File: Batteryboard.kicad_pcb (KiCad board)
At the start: 4 copper layers, 76.2 x 76.2 mm, 173 parts, among them IC1 FAN4010IL6X_F113, IC2 FAN4010IL6X_F113, IC3 FAN4010IL6X_F113, J1 Conn_01x02_Male, J2 Conn_01x03_Male, J3 Conn_01x05_Male, J4 Conn_01x02_Male, J5 SC_19-20, J6 Conn_01x04_Male, Q1 SI7617DN-T1-GE3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

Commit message: addede pms silkscreen
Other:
- board text added: "PMS Rev0"
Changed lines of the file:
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@@
   (general
     (thickness 1.6)
-    (drawings 6)
+    (drawings 7)
     (tracks 1505)
     (zones 0)
@@
   (page A4)
   (layers
-    (0 F.Cu signal)
-    (1 In1.Cu power)
-    (2 In2.Cu signal)
-    (31 B.Cu power)
+    (0 F.Cu signal hide)
+    (1 In1.Cu power hide)
+    (2 In2.Cu signal hide)
+    (31 B.Cu power hide)
     (32 B.Adhes user)
     (33 F.Adhes user)
@@
     )
   )
+  (gr_text "PMS Rev0" (at 249.1232 50.7492) (layer B.SilkS)
+    (effects (font (size 1.524 1.524) (thickness 0.254)) (justify mirror))
+  )
   (gr_circle (center 235.3818 63.0682) (end 273.1262 57.9882) (layer Edge.Cuts) (width 0.05))

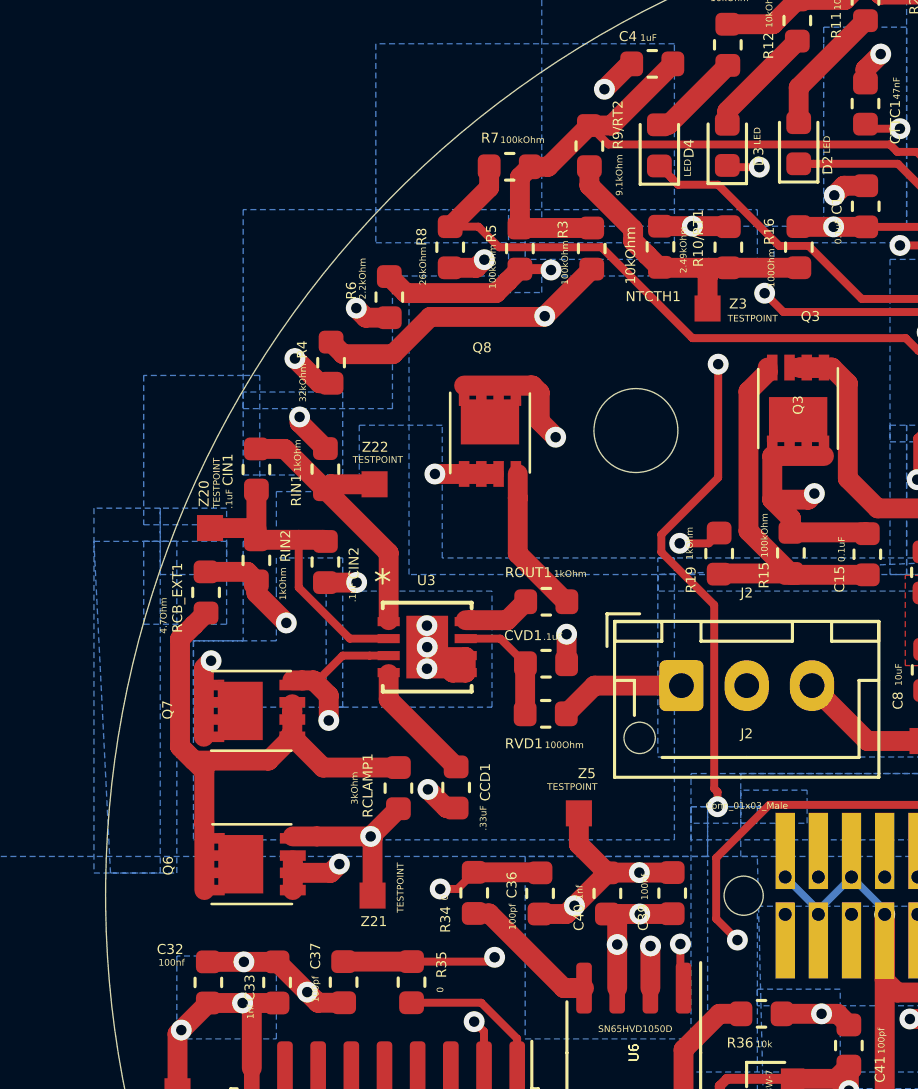
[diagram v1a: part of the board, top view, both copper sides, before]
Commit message: changed up balancing circuit cuz that no work and that bad
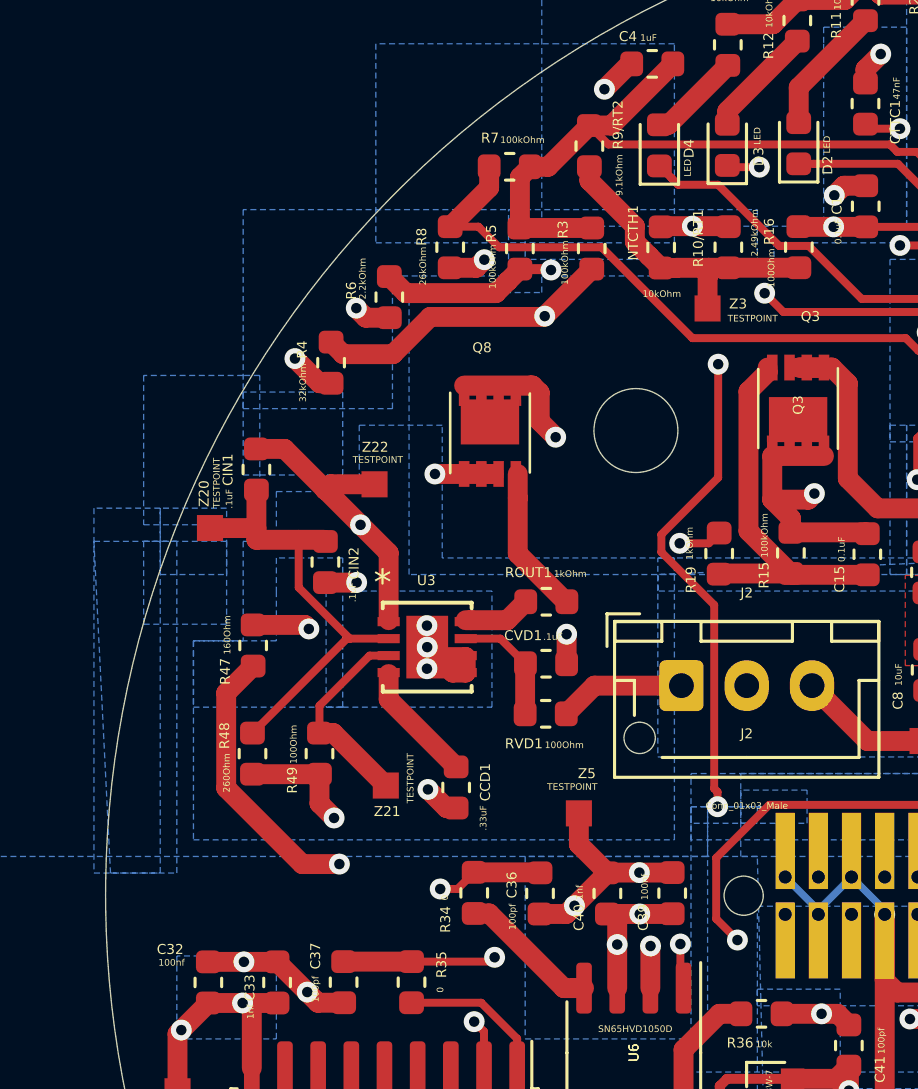
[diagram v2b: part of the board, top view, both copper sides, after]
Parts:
- removed Q6: SIS412DN-T1-GE3, SI7617DN-T1-GE3:SIS862DNT1GE3
- removed Q7: SI7617DN-T1-GE3, SI7617DN-T1-GE3:SIS862DNT1GE3
- removed RCB_EXT1: 4.7Ohm, Resistor_SMD:R_0603_1608Metric
- removed RCLAMP1: 3kOhm, Resistor_SMD:R_0603_1608Metric
- removed RIN1, RIN2: 1kOhm, Resistor_SMD:R_0603_1608Metric
- added R47: 160Ohm, Resistor_SMD:R_0603_1608Metric, F.Cu at (202.9, 53.5)
- added R48: 260Ohm, Resistor_SMD:R_0603_1608Metric, F.Cu at (202.9, 57.7)
- added R49: 100Ohm, Resistor_SMD:R_0603_1608Metric, F.Cu at (205.5, 57.7)
- moved Z21 4.24 mm to (208.0, 55.9)
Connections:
- net Q6G renamed Net-(R49-Pad1)
- net Q6S renamed Net-(F2-Pad2)
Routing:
- net Q6D: track 22.2 -> 0.00 mm
- net Net-(F2-Pad2): track 90.4 -> 76.5 mm, vias 2 -> 1
- net Net-(R49-Pad1): track 18.6 -> 7.86 mm, vias 2 -> 0
- net Net-(CIN1-Pad1): track 11.3 -> 18.3 mm, vias 0 -> 2
- net Net-(CIN1-Pad2): track 12.4 -> 17.7 mm
- net PGND2: track 75.1 -> 72.2 mm, vias 32 -> 31
- net Net-(J2-Pad2): track 25.1 -> 23.9 mm

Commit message: made some finishing touches, should be complete now
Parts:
- removed the C23 at (239.5, 96.9)
- removed the C31 at (220.5, 96.0)
- removed the C45 at (235.2, 99.3)
- removed the C46 at (224.9, 97.4)
- removed the C48 at (220.5, 92.6)
- removed the C49 at (227.0, 94.0)
- R48: value 260Ohm -> 261Ohm
- moved Z15 2.57 mm to (220.5, 88.7)
- renumbered NTCTH1 to NTCTH1/NTCG163JF103FT1S1
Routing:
- net 5V0: track 43.3 -> 39.7 mm
- net VSS: track 137.8 -> 134.4 mm
- net TEMP_OUT: track 15.3 -> 12.8 mm

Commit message: fixed stuff
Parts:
- removed J5: SC_19-20, MASA-LIB:bottom_Stack_Connector_2019_2020
- added J7: SC_19-20, MASA_Library:Stack_Connector_2019_2020, F.Cu at (235.4, 63.1)
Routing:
- net VSS: track 134.4 -> 122.0 mm
- net 5V0: track 39.7 -> 31.2 mm, vias 15 -> 14
- net CAN_L: track 36.7 -> 34.6 mm, vias 3 -> 2
- net CAN_H: track 33.2 -> 31.1 mm, vias 3 -> 2
- net 3V3: vias 3 -> 2
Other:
- net class Default: clearance 0.15 -> 0.1524
- rule trace_clearance: 0.15 -> 0.1524

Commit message: fixed some shit
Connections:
- IC1 pad 2: Net-(IC1-Pad2) -> (no net)
- IC1 pad 4: Net-(IC1-Pad4) -> (no net)
- IC2 pad 2: Net-(IC2-Pad2) -> (no net)
- IC2 pad 4: Net-(IC2-Pad4) -> (no net)
- IC3 pad 2: Net-(IC3-Pad2) -> (no net)
- IC3 pad 4: Net-(IC3-Pad4) -> (no net)
- J7 pad 1: VSS -> PGND2
- J7 pad 10: Net-(J7-Pad10) -> (no net)
- J7 pad 11: Net-(J7-Pad11) -> (no net)
- J7 pad 12: Net-(J7-Pad12) -> (no net)
- J7 pad 13: Net-(J7-Pad13) -> (no net)
- J7 pad 14: Net-(J7-Pad14) -> (no net)
- J7 pad 15: Net-(J7-Pad15) -> (no net)
- J7 pad 16: Net-(J7-Pad16) -> (no net)
- J7 pad 17: Net-(J7-Pad17) -> (no net)
- J7 pad 18: Net-(J7-Pad18) -> (no net)
- J7 pad 19: VSS -> PGND2
- J7 pad 20: VSS -> PGND2
- J7 pad 22: Net-(J7-Pad22) -> (no net)
- J7 pad 24: Net-(J7-Pad24) -> (no net)
- J7 pad 25: UART1_TX -> (no net)
- J7 pad 26: Net-(J7-Pad26) -> (no net)
- J7 pad 27: UART1_RX -> (no net)
- J7 pad 28: Net-(J7-Pad28) -> (no net)
- J7 pad 29: Net-(J7-Pad29) -> (no net)
- J7 pad 30: Net-(J7-Pad30) -> (no net)
- J7 pad 31: Net-(J7-Pad31) -> (no net)
- J7 pad 32: Net-(J7-Pad32) -> (no net)
- J7 pad 33: Net-(J7-Pad33) -> (no net)
- J7 pad 36: VSS -> PGND2
- J7 pad 37: VSS -> PGND2
- J7 pad 4: VSS -> PGND2
- J7 pad 40: VSS -> PGND2
- J7 pad 5: VSS -> PGND2
- J7 pad 8: Net-(J7-Pad8) -> (no net)
- J7 pad 9: Net-(J7-Pad9) -> (no net)
- U2 pad 12: Net-(U2-Pad12) -> (no net)
- U2 pad 13: Net-(U2-Pad13) -> (no net)
- U4 pad 15: Net-(U4-Pad15) -> (no net)
- U4 pad 16: Net-(U4-Pad16) -> (no net)
- U5 pad 3: Net-(U5-Pad3) -> (no net)
- U5 pad 7: Net-(U5-Pad7) -> (no net)
- U5 pad 8: Net-(U5-Pad8) -> (no net)
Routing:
- net VSS: track 122.0 -> 145.3 mm, vias 54 -> 52
- net PGND2: track 72.2 -> 85.0 mm
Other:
- net class Default: clearance 0.1524 -> 0.14986
- rule trace_clearance: 0.1524 -> 0.14986

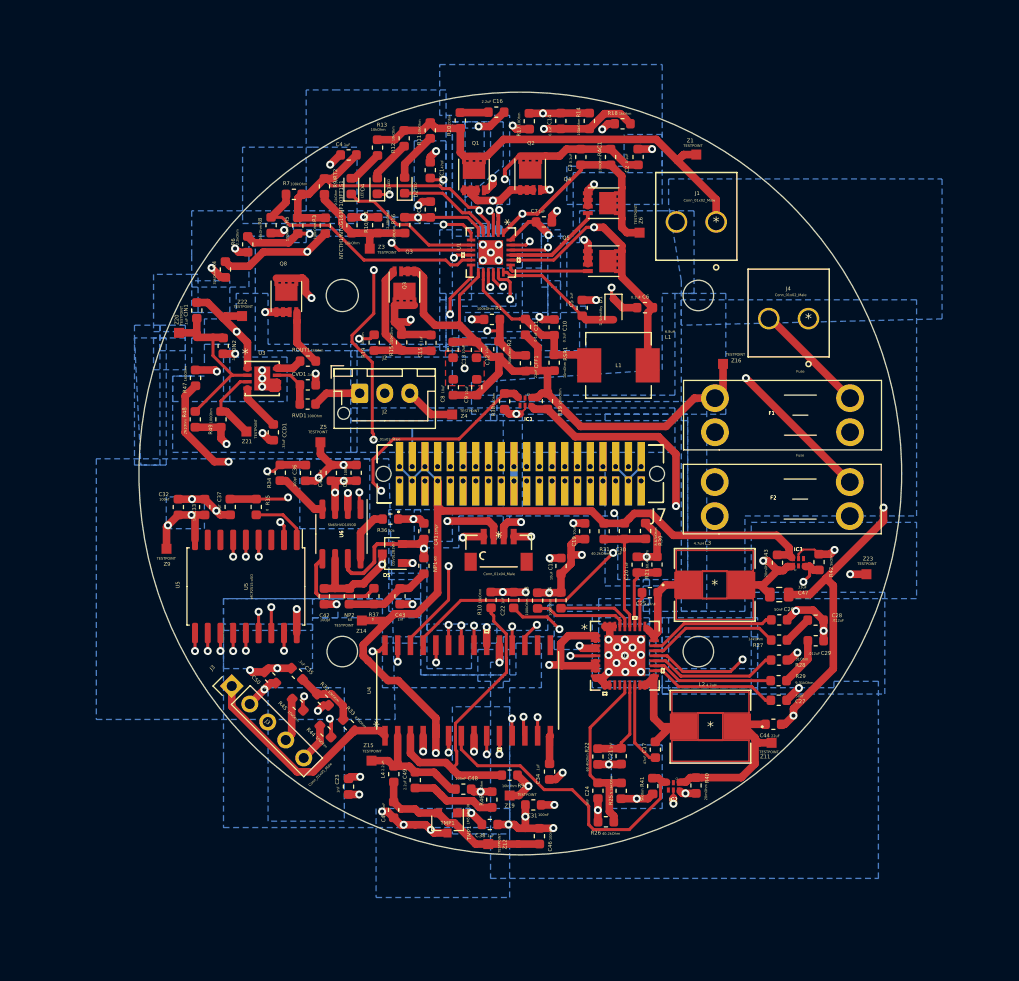
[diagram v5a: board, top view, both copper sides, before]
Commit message: added ground pours
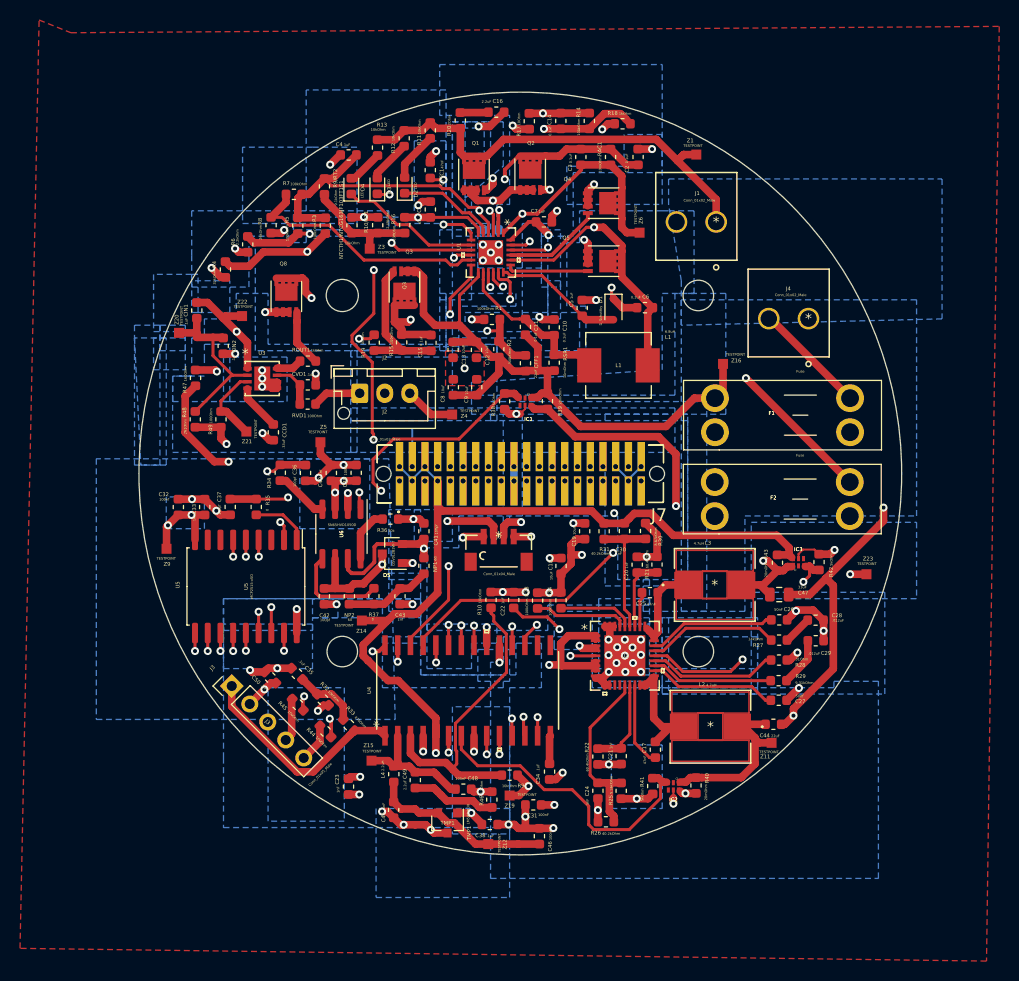
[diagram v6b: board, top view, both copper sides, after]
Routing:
- added copper zone on In2.Cu, net PGND2
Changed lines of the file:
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@@
   )
   (setup
-    (last_trace_width 0.762)
+    (last_trace_width 0.2)
     (user_trace_width 0.2)
     (user_trace_width 0.2032)
@@
   (segment (start 228.5746 57.1754) (end 226.4645 57.1754) (width 0.762) (layer F.Cu) (net 43))
   (via (at 238.3156 71.5136) (size 0.8) (drill 0.4) (layers F.Cu B.Cu) (net 43))
+  (segment (start 234.7468 63.8124) (end 234.7468 62.3824) (width 0.762) (layer B.Cu) (net 43))
+  (segment (start 246.1768 63.6524) (end 244.9068 62.3824) (width 0.2) (layer B.Cu) (net 43))
+  (segment (start 246.1768 63.6524) (end 247.4468 62.3824) (width 0.2) (layer B.Cu) (net 43))
+  (segment (start 246.1768 63.8124) (end 246.1768 63.6524) (width 0.2) (layer B.Cu) (net 43))
+  (segment (start 225.8568 63.6524) (end 224.5868 62.3824) (width 0.2) (layer In2.Cu) (net 43))
+  (segment (start 225.8568 63.8124) (end 225.8568 63.6524) (width 0.2) (layer In2.Cu) (net 43))
+  (segment (start 223.3168 63.6524) (end 224.5868 62.3824) (width 0.2) (layer In2.Cu) (net 43))
+  (segment (start 223.3168 63.8124) (end 223.3168 63.6524) (width 0.2) (layer In2.Cu) (net 43))
+  (segment (start 224.5868 62.3824) (end 224.5868 58.6232) (width 0.2) (layer B.Cu) (net 43))
   (segment (start 245.333483 77.718883) (end 245.333483 78.3423) (width 0.3048) (layer F.Cu) (net 44))
   (segment (start 244.87211 77.25751) (end 245.333483 77.718883) (width 0.3048) (layer F.Cu) (net 44))
@@
   (segment (start 218.817094 88.743694) (end 221.357094 88.743694) (width 0.762) (layer F.Cu) (net 67))
   (segment (start 218.410508 89.15028) (end 218.817094 88.743694) (width 0.762) (layer F.Cu) (net 67))
-  (segment (start 214.703684 92.857104) (end 218.410508 89.15028) (width 0.762) (layer F.Cu) (net 67))
   (segment (start 213.088822 92.857104) (end 214.703684 92.857104) (width 0.762) (layer F.Cu) (net 67))
   (segment (start 206.567498 86.33578) (end 213.088822 92.857104) (width 0.762) (layer F.Cu) (net 67))
   (segment (start 206.567498 84.291898) (end 206.567498 86.33578) (width 0.762) (layer F.Cu) (net 67))
+  (segment (start 214.703684 92.857104) (end 218.410508 89.15028) (width 0.762) (layer F.Cu) (net 67))
   (segment (start 215.215 66.635) (end 215.615 66.635) (width 0.762) (layer F.Cu) (net 68))
   (segment (start 214.8425 66.635) (end 215.215 66.635) (width 0.762) (layer F.Cu) (net 68))
@@
   (segment (start 238.53 37.94) (end 238.53 37.3521) (width 0.762) (layer F.Cu) (net 95))
   (segment (start 238.53 37.3521) (end 239.0521 36.83) (width 0.762) (layer F.Cu) (net 95))
-  (segment (start 234.7468 63.8124) (end 234.7468 62.3824) (width 0.762) (layer B.Cu) (net 43))
-  (segment (start 246.1768 63.6524) (end 244.9068 62.3824) (width 0.2) (layer B.Cu) (net 43))
-  (segment (start 246.1768 63.6524) (end 247.4468 62.3824) (width 0.2) (layer B.Cu) (net 43))
-  (segment (start 246.1768 63.8124) (end 246.1768 63.6524) (width 0.2) (layer B.Cu) (net 43))
-  (segment (start 225.8568 63.6524) (end 224.5868 62.3824) (width 0.2) (layer In2.Cu) (net 43))
-  (segment (start 225.8568 63.8124) (end 225.8568 63.6524) (width 0.2) (layer In2.Cu) (net 43))
-  (segment (start 223.3168 63.6524) (end 224.5868 62.3824) (width 0.2) (layer In2.Cu) (net 43))
-  (segment (start 223.3168 63.8124) (end 223.3168 63.6524) (width 0.2) (layer In2.Cu) (net 43))
-  (segment (start 224.5868 62.3824) (end 224.5868 58.6232) (width 0.2) (layer B.Cu) (net 43))
   (via (at 230.5304 47.6758) (size 0.8) (drill 0.4) (layers F.Cu B.Cu) (net 95))
   (segment (start 231.7625 47.68) (end 230.5346 47.68) (width 0.762) (layer F.Cu) (net 95))
@@
       )
     )
+  )
+  (zone (net 43) (net_name PGND2) (layer F.Cu) (hatch edge 0.508)
+    (connect_pads (clearance 0.508))
+    (min_thickness 0.254)
+    (fill yes (arc_segments 32) (thermal_gap 0.508) (thermal_bridge_width 0.508))
+    (polygon
+      (pts
+        (xy 190.5 19.05) (xy 283.21 18.415) (xy 281.94 111.76) (xy 185.42 110.49) (xy 187.325 17.78)
+      )
+    )
+  )
+  (zone (net 43) (net_name PGND2) (layer In2.Cu) (hatch edge 0.508)
+    (connect_pads (clearance 0.508))
+    (min_thickness 0.254)
+    (fill yes (arc_segments 32) (thermal_gap 0.508) (thermal_bridge_width 0.508))
+    (polygon
+      (pts
+        (xy 175.895 6.35) (xy 177.8 116.205) (xy 292.735 117.475) (xy 290.195 9.525) (xy 177.165 6.35)
+      )
+    )
